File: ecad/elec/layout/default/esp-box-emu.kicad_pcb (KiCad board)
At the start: 2 copper layers, 147.3 x 76.4 mm, 27 parts

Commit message: working on layout and ci
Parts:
- added C1: 25V 10uF X5R ±10% 0805 Multilayer Ceramic Capacitors MLCC -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, lib:C0805, F.Cu at (15.7, 6.01)
- added C2: 25V 10uF X5R ±10% 0805 Multilayer Ceramic Capacitors MLCC -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, lib:C0805, F.Cu at (9.22, 6.01)
- added C3: 25V 10uF X5R ±10% 0805 Multilayer Ceramic Capacitors MLCC -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, lib:C0805, F.Cu at (15.7, 1.00)
- added C4: 25V 10uF X5R ±10% 0805 Multilayer Ceramic Capacitors MLCC -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, lib:C0805, F.Cu at (9.22, 1.00)
- added C5: 16V 100nF X7R ±10% 0402 Multilayer Ceramic Capacitors MLCC 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, lib:C0402, F.Cu at (18.3, 14.5)
- added L1: , lib:IND-SMD_L2.5-W2.0_WPN252012H, F.Cu at (2.09, 13.4)
- added LED1: , lib:LED0805-R-RD, F.Cu at (2.35, 8.04)
- added R22: 62.5mW Thick Film Resistors 50V ±100ppm/℃ ±1% 255Ω 0402 Chi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, lib:R0402, F.Cu at (8.46, 10.5)
- added R23: 62.5mW Thick Film Resistors 75V ±1% ±100ppm/℃ 249Ω 0402 Chi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, lib:R0402, F.Cu at (18.3, 10.5)
- added R5: 62.5mW Thick Film Resistors 50V ±100ppm/℃ ±1% 243kΩ 0402 Ch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, lib:R0402, F.Cu at (8.46, 18.5)
- added R6: 62.5mW Thick Film Resistors 50V ±100ppm/℃ ±0.5% 27.4kΩ 0402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, lib:R0402, F.Cu at (13.4, 18.5)
- added R7: 62.5mW Thick Film Resistors 50V ±100ppm/℃ ±1% 1MΩ 0402 Chip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, lib:R0402, F.Cu at (8.46, 14.5)
- added R8: 62.5mW Thick Film Resistors 50V ±100ppm/℃ ±1% 2kΩ 0402 Chip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, lib:R0402, F.Cu at (13.4, 14.5)
- added R9: 62.5mW Thick Film Resistors 50V ±100ppm/℃ ±1% 2.55kΩ 0402 C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, lib:R0402, F.Cu at (13.4, 10.5)
- added U3: , lib:VSON-14_L4.0-W3.0-P0.50-BL-EP_TI_DSJ, F.Cu at (2.25, 1.80)
- R1, R2: value 62.5mW Thick Film Resistors ±100ppm/℃ ±1% 5.1kΩ 0402 Chip Resistor - Surface Mount ROHS -> 62.5mW Thick Film Resistors 50V ±100ppm/℃ ±1% 4.7kΩ 0402 Chip Resistor - Surface Mount ROHS
- R10: renamed from R5; value 62.5mW Thick Film Resistors ±100ppm/℃ ±1% 10kΩ 0402 Chip Resistor - Surface Mount ROHS -> 62.5mW Thick Film Resistors 50V ±100ppm/℃ ±1% 10kΩ 0402 Chip Resistor - Surface Mount ROHS
- R11: renamed from R6; value 62.5mW Thick Film Resistors ±100ppm/℃ ±1% 10kΩ 0402 Chip Resistor - Surface Mount ROHS -> 62.5mW Thick Film Resistors 50V ±100ppm/℃ ±1% 10kΩ 0402 Chip Resistor - Surface Mount ROHS
- R12: renamed from R7; value 62.5mW Thick Film Resistors ±100ppm/℃ ±1% 10kΩ 0402 Chip Resistor - Surface Mount ROHS -> 62.5mW Thick Film Resistors 50V ±100ppm/℃ ±1% 10kΩ 0402 Chip Resistor - Surface Mount ROHS
- R13: renamed from R8; value 62.5mW Thick Film Resistors ±100ppm/℃ ±1% 10kΩ 0402 Chip Resistor - Surface Mount ROHS -> 62.5mW Thick Film Resistors 50V ±100ppm/℃ ±1% 10kΩ 0402 Chip Resistor - Surface Mount ROHS
- R14: renamed from R9; value 62.5mW Thick Film Resistors ±100ppm/℃ ±1% 10kΩ 0402 Chip Resistor - Surface Mount ROHS -> 62.5mW Thick Film Resistors 50V ±100ppm/℃ ±1% 10kΩ 0402 Chip Resistor - Surface Mount ROHS
- R15: renamed from R10; value 62.5mW Thick Film Resistors ±100ppm/℃ ±1% 10kΩ 0402 Chip Resistor - Surface Mount ROHS -> 62.5mW Thick Film Resistors 50V ±100ppm/℃ ±1% 10kΩ 0402 Chip Resistor - Surface Mount ROHS
- R16: renamed from R11; value 62.5mW Thick Film Resistors ±100ppm/℃ ±1% 10kΩ 0402 Chip Resistor - Surface Mount ROHS -> 62.5mW Thick Film Resistors 50V ±100ppm/℃ ±1% 10kΩ 0402 Chip Resistor - Surface Mount ROHS
- R17: renamed from R12; value 62.5mW Thick Film Resistors ±100ppm/℃ ±1% 10kΩ 0402 Chip Resistor - Surface Mount ROHS -> 62.5mW Thick Film Resistors 50V ±100ppm/℃ ±1% 10kΩ 0402 Chip Resistor - Surface Mount ROHS
- R18: renamed from R13; value 62.5mW Thick Film Resistors ±100ppm/℃ ±1% 10kΩ 0402 Chip Resistor - Surface Mount ROHS -> 62.5mW Thick Film Resistors 50V ±100ppm/℃ ±1% 10kΩ 0402 Chip Resistor - Surface Mount ROHS
- R19: renamed from R14; value 62.5mW Thick Film Resistors ±100ppm/℃ ±1% 10kΩ 0402 Chip Resistor - Surface Mount ROHS -> 62.5mW Thick Film Resistors 50V ±100ppm/℃ ±1% 10kΩ 0402 Chip Resistor - Surface Mount ROHS
- R20: renamed from R15; value 62.5mW Thick Film Resistors ±100ppm/℃ ±1% 10kΩ 0402 Chip Resistor - Surface Mount ROHS -> 62.5mW Thick Film Resistors 50V ±100ppm/℃ ±1% 10kΩ 0402 Chip Resistor - Surface Mount ROHS
- R21: renamed from R16; value 62.5mW Thick Film Resistors ±100ppm/℃ ±1% 10kΩ 0402 Chip Resistor - Surface Mount ROHS -> 62.5mW Thick Film Resistors 50V ±100ppm/℃ ±1% 10kΩ 0402 Chip Resistor - Surface Mount ROHS
- R3, R4: value 62.5mW Thick Film Resistors ±100ppm/℃ ±1% 10kΩ 0402 Chip Resistor - Surface Mount ROHS -> 62.5mW Thick Film Resistors 50V ±100ppm/℃ ±1% 10kΩ 0402 Chip Resistor - Surface Mount ROHS
- renumbered U3 to U10, U4 to U11, U5 to U12, U6 to U4, U7 to U5, U8 to U6, U9 to U7, U10 to U8, U11 to U9
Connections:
- net pmod1-_1 renamed _1
- net pmod1-_3 renamed _3
- net pmod2-_6 renamed _6
- R3 pad 2: i2c_pullup.r_sda-vcc -> vcc
- R4 pad 2: i2c_pullup.r_sda-vcc -> vcc
- U10 pad 6: pmod1-_6 -> scl
- U10 pad 8: pmod1-_8 -> sda
- U11 pad 1: pmod2-_1 -> cs
- U11 pad 3: pmod2-_3 -> mosi
- U11 pad 5: _5 -> miso
- U11 pad 7: _7 -> sck
- U11 pad 8: pmod2-_8 -> battery_measurement
- U12 pad 1: pin2x2-_1 -> vcc-1
- U12 pad 2: pin2x2-_2 -> gnd
- U12 pad 3: pin2x2-_3 -> gnd
- U12 pad 4: pin2x2-_4 -> vcc-1
- U4 pad 1: stat -> mcp73831-gnd
- U4 pad 4: vcc-1 -> vcc-3
- U4 pad 5: gnd -> prog
- U6 pad 2: dat3 -> cs
- U6 pad 3: cmd -> mosi
- U6 pad 5: clk -> sck
- U6 pad 7: dat0 -> miso

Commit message: working on buttons
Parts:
- moved C1 128.4 mm to (108.7, 94.6)
- moved C2 128.4 mm to (102.2, 94.6)
- moved C3 128.4 mm to (108.7, 89.5)
- moved C4 128.4 mm to (102.2, 89.5)
- moved C5 128.4 mm to (111.2, 103.0)
- moved L1 128.4 mm to (95.1, 101.9)
- moved LED1 128.4 mm to (95.3, 96.6)
- moved R22 128.4 mm to (101.4, 99.1)
- moved R23 128.4 mm to (111.2, 99.1)
- moved R5 128.4 mm to (101.4, 107.0)
- moved R6 128.4 mm to (106.3, 107.0)
- moved R7 128.4 mm to (101.4, 103.0)
- moved R8 128.4 mm to (106.3, 103.0)
- moved R9 128.4 mm to (106.3, 99.1)
- moved U3 125.0 mm to (97.6, 82.7)
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
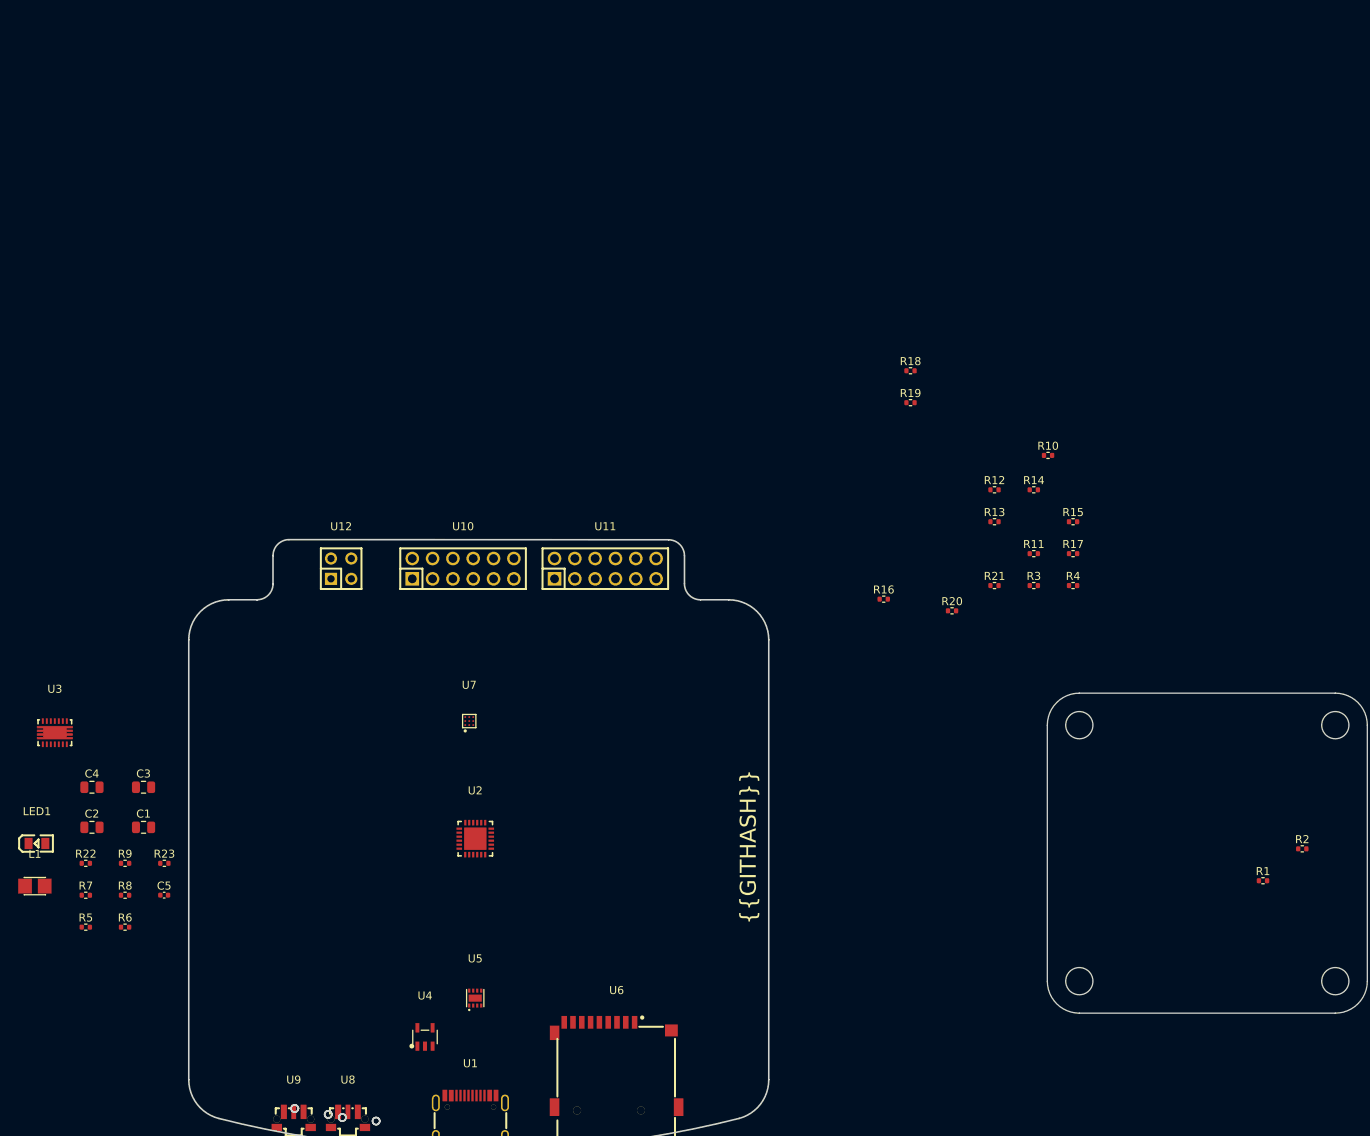
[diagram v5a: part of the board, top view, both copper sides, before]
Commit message: WIP updating how buttons are setup and adding layouts for gbc start/select a/b and dpad buttons
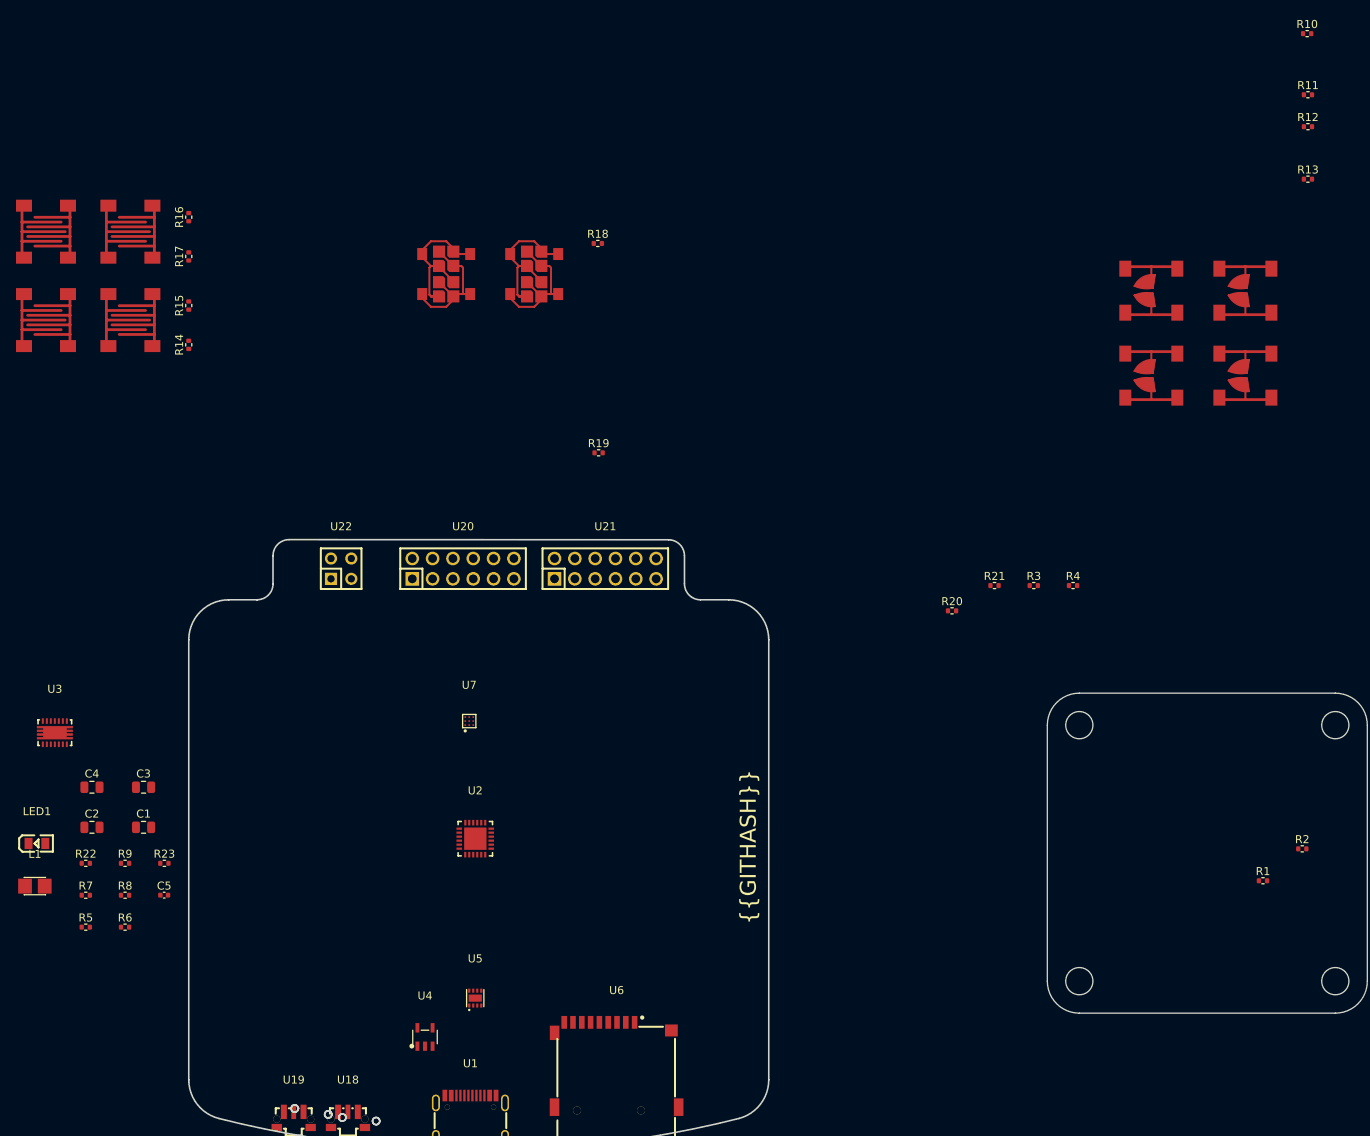
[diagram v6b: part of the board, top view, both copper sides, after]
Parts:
- added U10: , lib:GBC_DPAD_BUTTON, F.Cu at (234.6, 27.5)
- added U11: , lib:GBC_DPAD_BUTTON, F.Cu at (246.4, 27.5)
- added U12: , lib:GBC_A_B_BUTTON, F.Cu at (96.5, 20.1)
- added U13: , lib:GBC_A_B_BUTTON, F.Cu at (107.0, 20.1)
- added U14: , lib:GBC_A_B_BUTTON, F.Cu at (107.0, 31.2)
- added U15: , lib:GBC_A_B_BUTTON, F.Cu at (96.5, 31.2)
- added U16: , lib:GBC_START_SELECT_BUTTON, F.Cu at (146.5, 25.4)
- added U17: , lib:GBC_START_SELECT_BUTTON, F.Cu at (157.5, 25.4)
- added U8: , lib:GBC_DPAD_BUTTON, F.Cu at (234.6, 38.1)
- added U9: , lib:GBC_DPAD_BUTTON, F.Cu at (246.4, 38.1)
- moved R17 116.6 mm to (114.3, 23.2), turned to 90 degrees
- moved R15 113.8 mm to (114.3, 29.3), turned to 90 degrees
- moved R14 107.2 mm to (114.3, 34.2), turned to 90 degrees
- moved R16 99.1 mm to (114.3, 18.3), turned to 90 degrees
- moved R11 66.8 mm to (254.2, 2.99)
- moved R10 61.9 mm to (254.1, -4.65)
- moved R12 60.0 mm to (254.2, 6.98)
- moved R13 58.0 mm to (254.2, 13.5)
- moved R18 42.2 mm to (165.4, 21.6)
- moved R19 39.5 mm to (165.5, 47.7)
- renumbered U8 to U18, U9 to U19, U10 to U20, U11 to U21, U12 to U22
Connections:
- R10 pad 1: vcc -> gnd
- R11 pad 1: vcc -> gnd
- R12 pad 1: vcc -> gnd
- R13 pad 1: vcc -> gnd

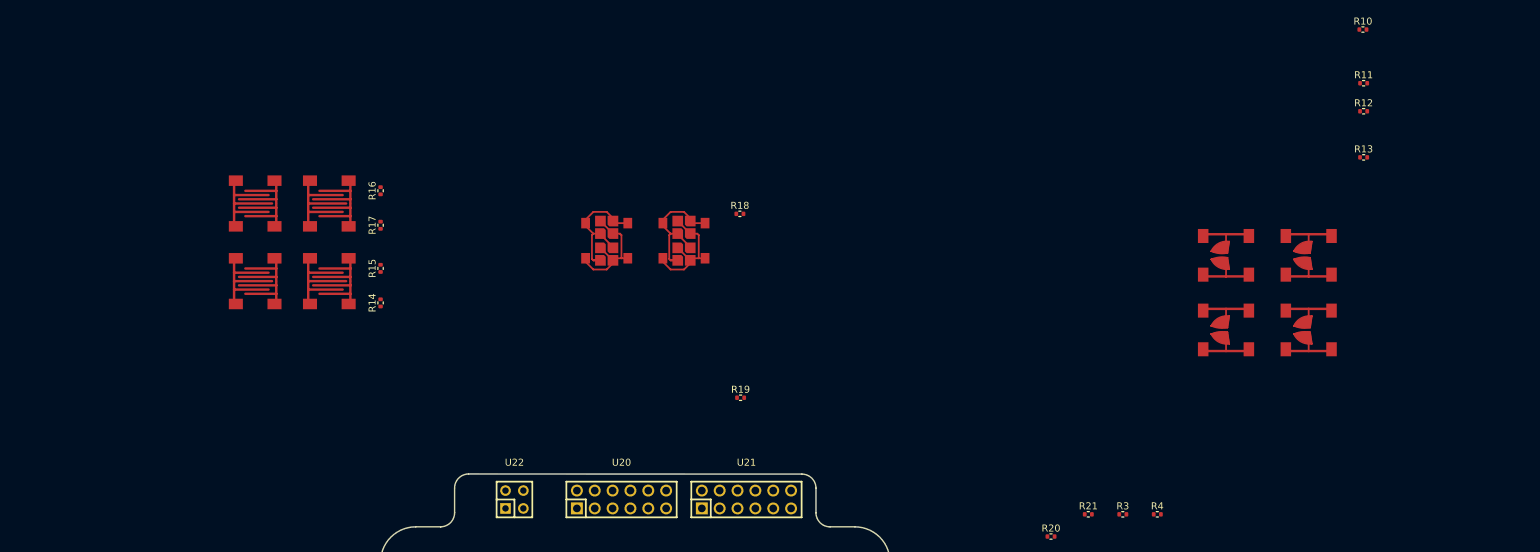
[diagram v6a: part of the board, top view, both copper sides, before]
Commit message: udpate layout to have properly positioned buttons
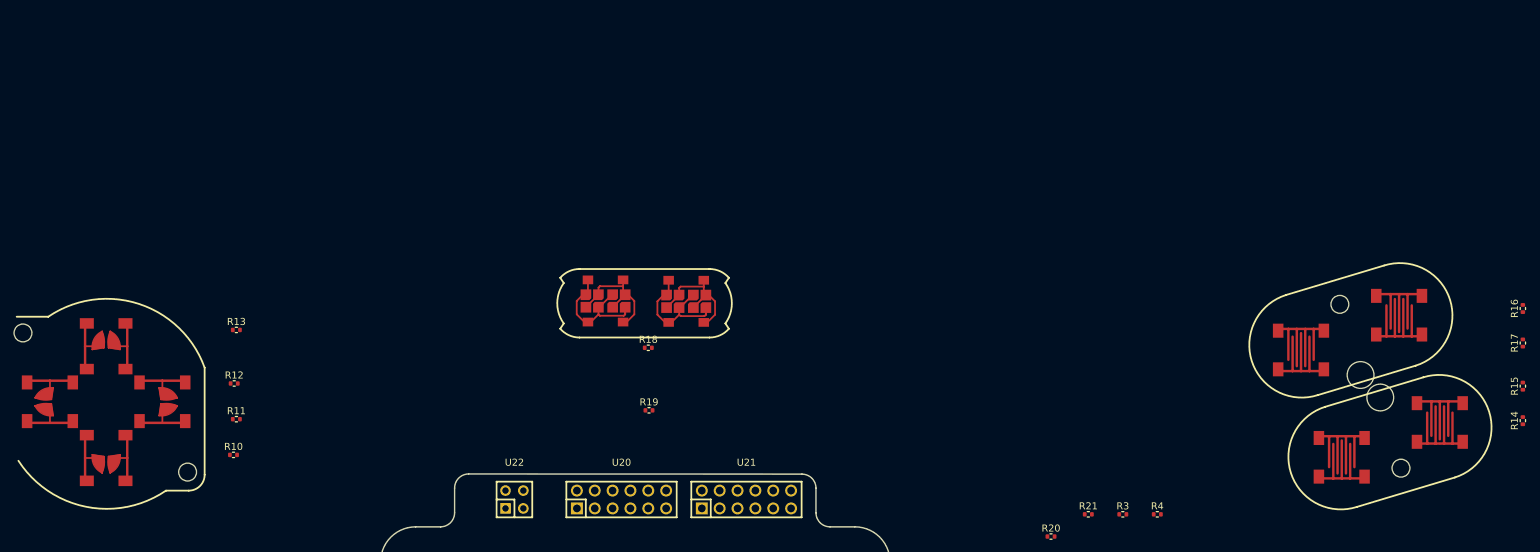
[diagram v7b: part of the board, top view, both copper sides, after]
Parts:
- added @HOLE10: , , B.Cu at (63.4, 38.5)
- added @HOLE11: , , B.Cu at (256.6, 47.7)
- added @HOLE11: , , B.Cu at (253.8, 44.5)
- added @HOLE7: , , B.Cu at (86.8, 58.3)
- added @HOLE9: , , B.Cu at (259.5, 57.8)
- added @HOLE9: , , B.Cu at (250.8, 34.5)
- moved U9 172.1 mm to (75.2, 56.3), turned to 90 degrees
- moved R10 171.7 mm to (93.4, 55.9)
- moved U10 168.7 mm to (67.2, 48.3)
- moved R11 167.4 mm to (93.8, 50.8)
- moved R12 165.3 mm to (93.5, 45.7)
- moved U11 164.5 mm to (83.2, 48.3), turned to 180 degrees
- moved R14 163.4 mm to (276.9, 51.0)
- moved R15 163.4 mm to (276.9, 46.1)
- moved R16 163.4 mm to (276.9, 35.0)
- moved R17 163.4 mm to (276.9, 40.0)
- moved R13 162.3 mm to (93.8, 38.1)
- moved U13 161.1 mm to (265.0, 51.3), turned to 0 degrees
- moved U8 159.4 mm to (75.2, 40.4), turned to -90 degrees
- moved U12 158.8 mm to (251.1, 56.2), turned to 180 degrees
- moved U14 152.3 mm to (259.2, 36.0), turned to 0 degrees
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
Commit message: update layout
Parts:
- moved R2 106.2 mm to (151.3, 126.1), turned to 90 degrees
- moved R1 103.3 mm to (148.3, 126.1), turned to 90 degrees
- moved R4 92.4 mm to (137.2, 93.5), turned to -90 degrees
- moved R3 85.4 mm to (139.7, 93.5), turned to -90 degrees
- moved R21 62.7 mm to (160.0, 94.5), turned to 90 degrees
- moved R20 58.6 mm to (160.0, 98.5), turned to -90 degrees
- moved U3 45.6 mm to (123.2, 120.5)
- moved C4 42.2 mm to (122.7, 126.5), turned to 180 degrees
- moved C3 37.7 mm to (122.6, 124.5), turned to 180 degrees
- moved L1 37.0 mm to (127.0, 120.6), turned to 90 degrees
- moved C2 29.2 mm to (122.8, 115.3), turned to 180 degrees
- moved R5 27.2 mm to (123.4, 123.0), turned to 180 degrees
- moved C1 26.8 mm to (122.8, 117.3), turned to 180 degrees
- moved R7 24.4 mm to (119.9, 119.0), turned to 180 degrees
- moved R6 22.0 mm to (121.5, 123.0), turned to 180 degrees
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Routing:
- net vcc-1: track 0.00 -> 6.20 mm
- net vcc-2: track 0.00 -> 5.63 mm
- net l1: track 0.00 -> 2.59 mm
- net l2: track 0.00 -> 2.54 mm
- net out: track 0.00 -> 2.08 mm
- net gnd: track 0.00 -> 1.99 mm
- net cc2: track 0.00 -> 1.65 mm
- net cc1: track 0.00 -> 1.60 mm
- net vina: track 0.00 -> 1.41 mm
- net pg: track 0.00 -> 1.29 mm
